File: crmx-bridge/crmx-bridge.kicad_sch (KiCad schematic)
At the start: 77 parts, among them IC101 ESP32-S3-WROOM-1U-N4R2, J102 NC3FAAH2, J103 USB_C_Receptacle_USB2.0_16P, J104 NC3MAAH, J105 Conn_01x02_Pin, J106 AFC07-S16FCC-00, Q101 DMP4025SFGQ-13, Q102 AO3400A, U101 TIMOTWO, U102 AP63200WU, U103 ISO3088DW, U104 SRV05-4, U105 ISO3088DW, U106 TEA1-0505

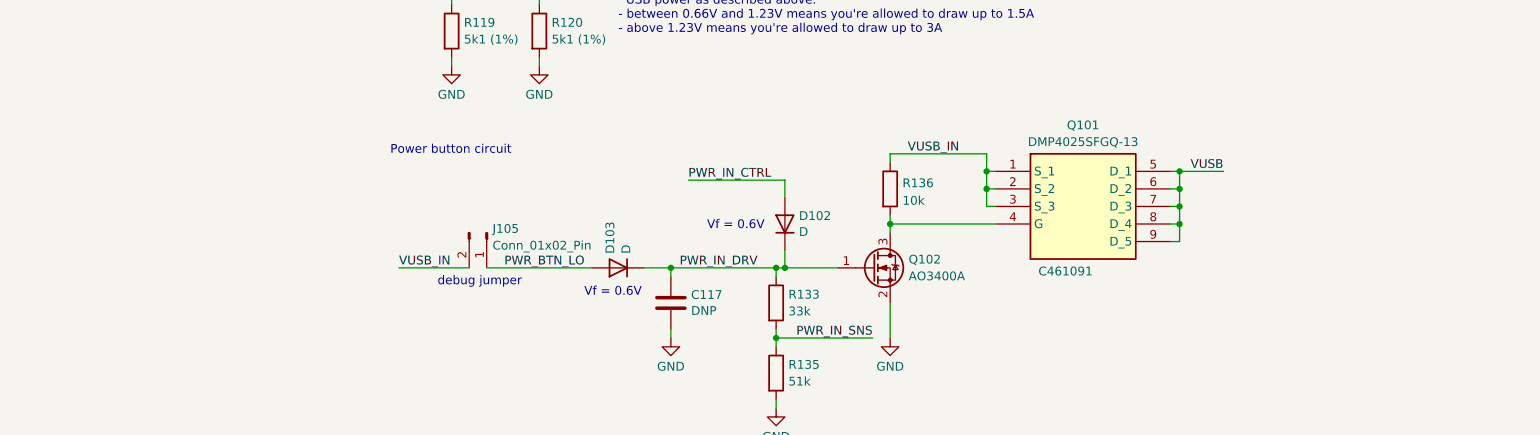
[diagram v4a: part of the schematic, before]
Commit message: Get settings working on display
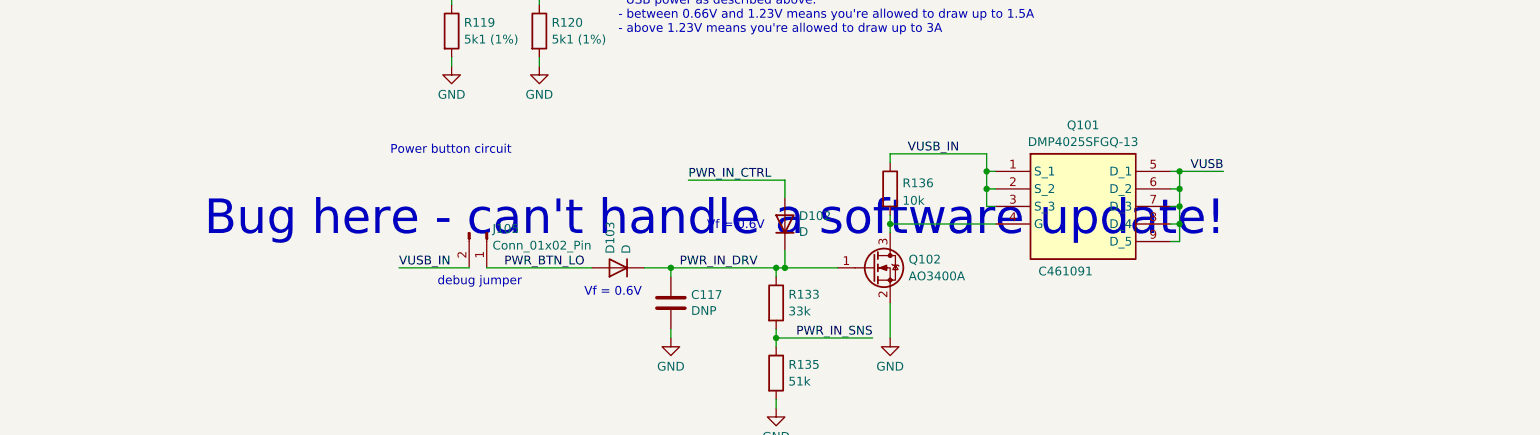
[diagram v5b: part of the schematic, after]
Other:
- note added: "Bug here - can't handle a software update!"
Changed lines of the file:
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@@
+		)
+	)
+	(text "Bug here - can't handle a software update!"
+		(exclude_from_sim no)
+		(at 68.58 224.028 0)
+		(effects
+			(font
+				(size 5 5)
+			)
 		)
 	)
